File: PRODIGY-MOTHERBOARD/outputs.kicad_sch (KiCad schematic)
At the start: 19 parts, among them J10 GPIO, J11 SPI_OUT, J12 I2C, J13 CAN, J14 SERIAL, J15 12V OUT, J16 SERVO, J17 SERVO, J18 SERVO, J19 Ultrasonic, J20 MOTOR, J21 MOTOR, J3 A_IN, J4 USB_A, J5 A_OUT, J6 Neopixel, J7 GPIO, J8 GPIO, J9 GPIO

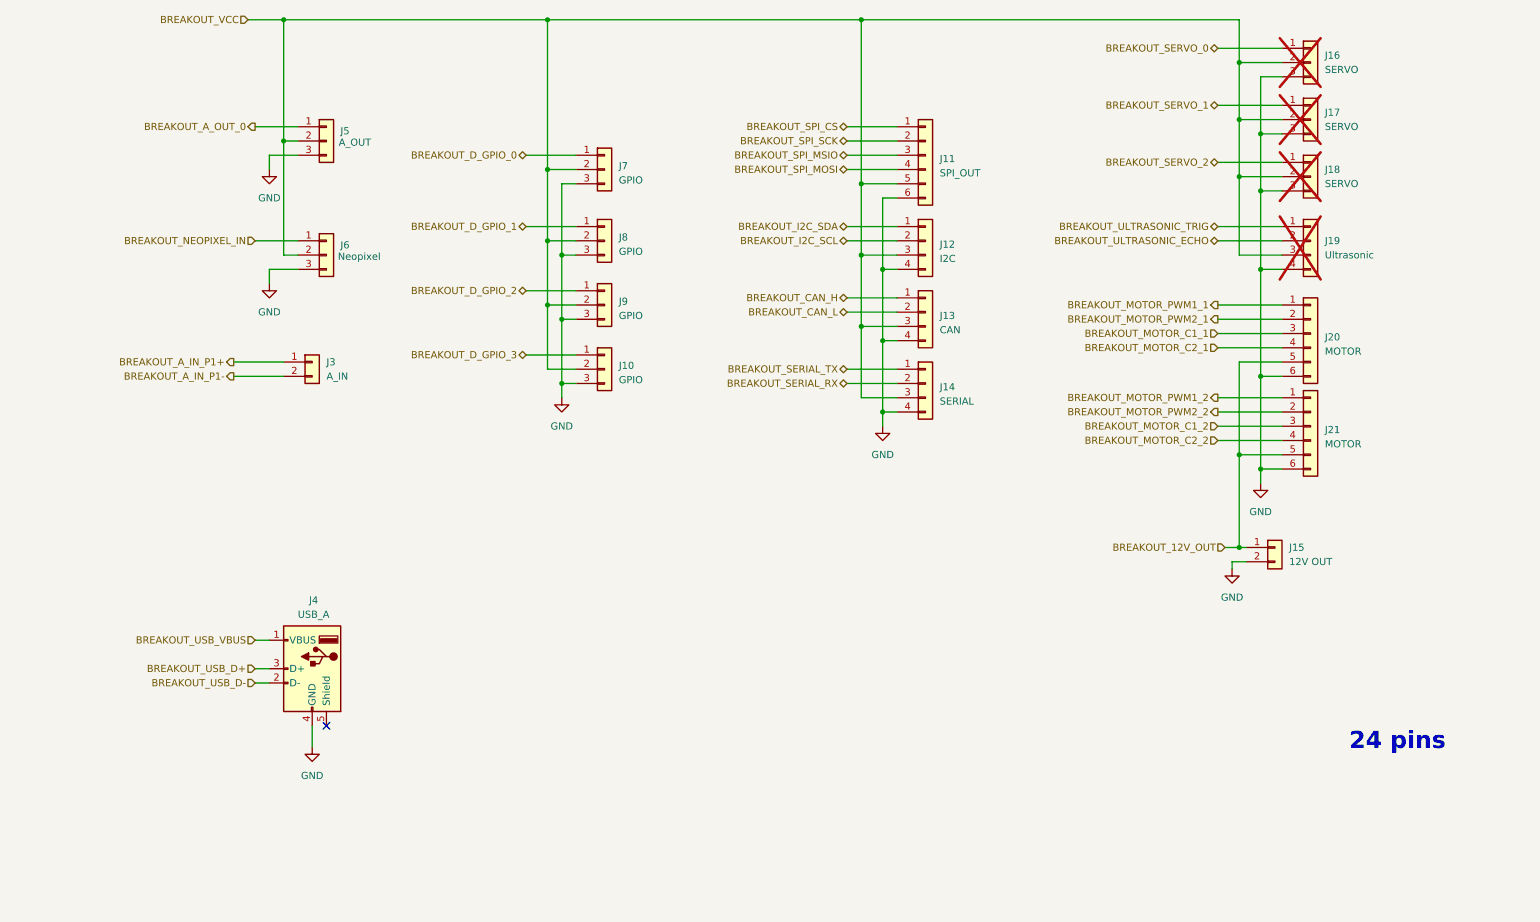
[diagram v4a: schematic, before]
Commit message: Analog schematic finished, except the joystick part.
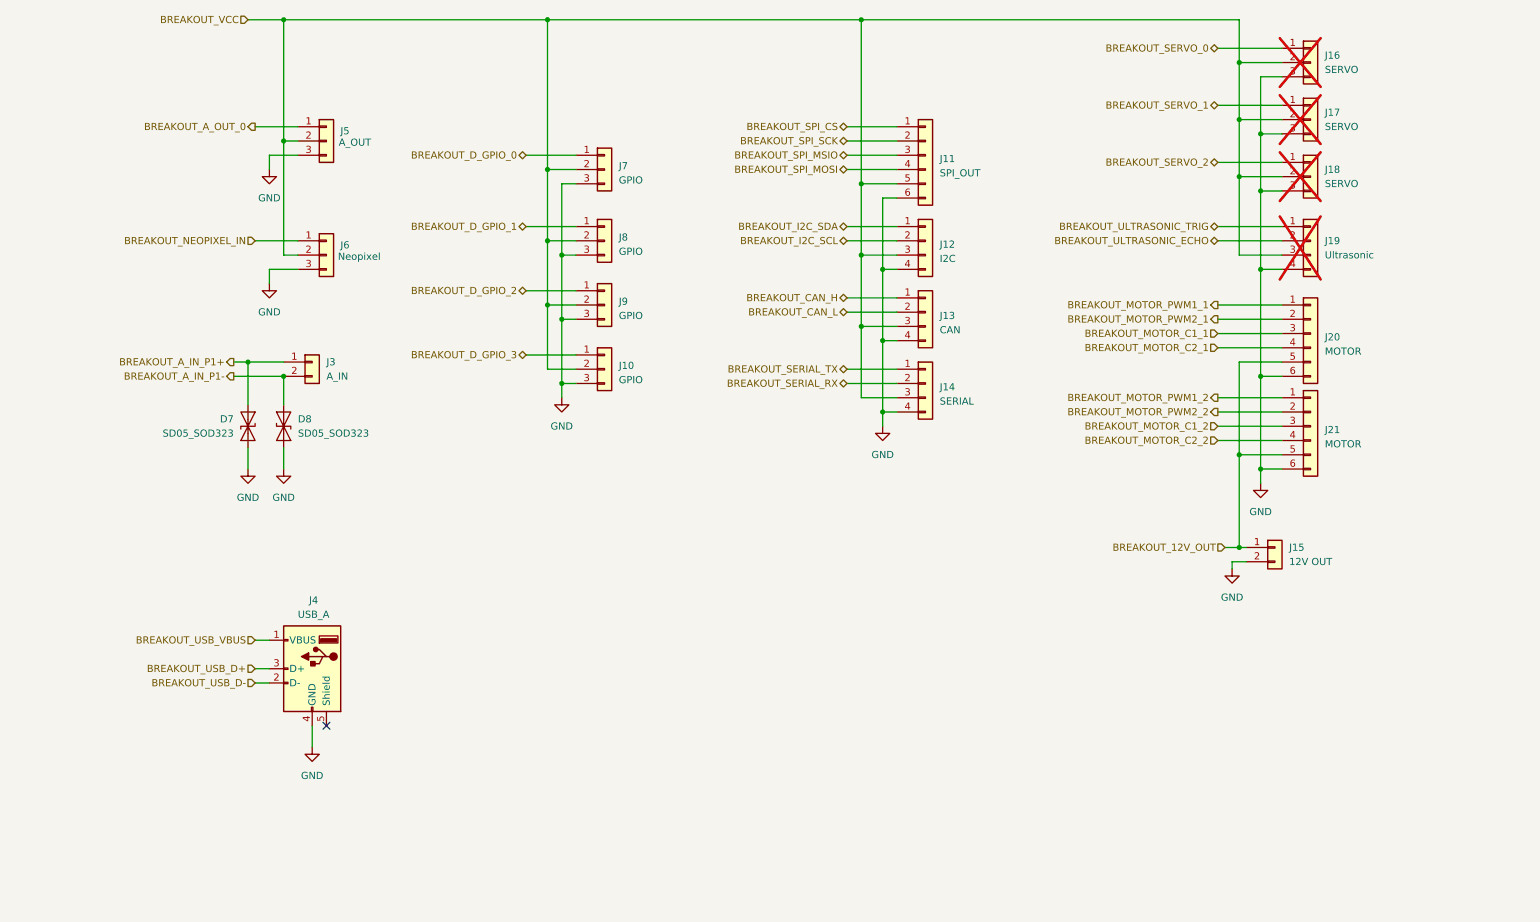
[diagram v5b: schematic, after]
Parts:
- added D7, D8: SD05_SOD323, Diode_SMD:D_SOD-323, symbol Diode:SD05_SOD323
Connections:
- net BREAKOUT_A_IN_P1+: now also D7.2 (A2)
- net BREAKOUT_A_IN_P1-: now also D8.2 (A2)
- net GND: now also D7.1 (A1), D8.1 (A1)
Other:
- note removed: "24 pins"

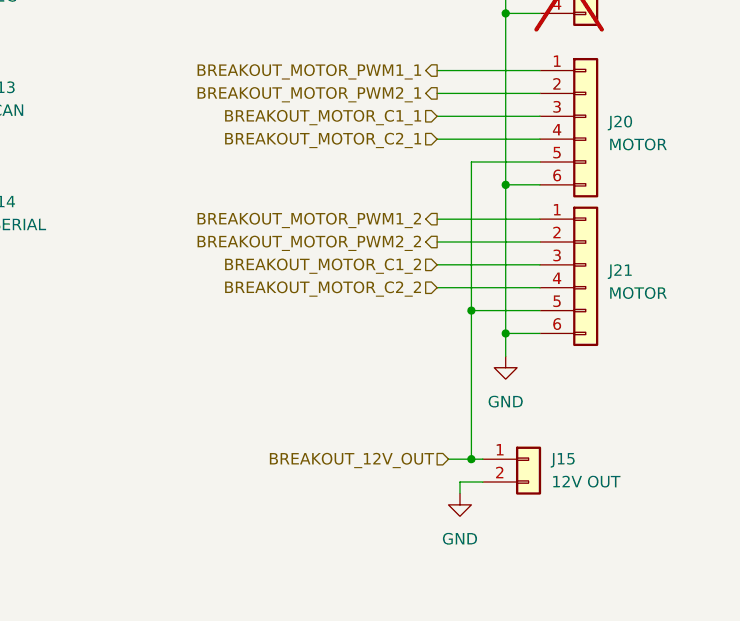
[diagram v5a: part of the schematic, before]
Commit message: Added pins to MCU. Added Decoder for SPI SS-Multiplexing.
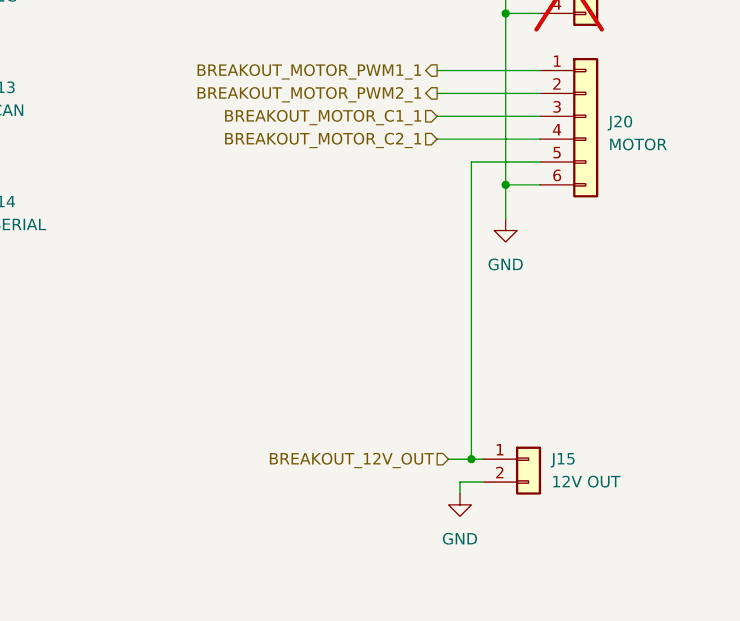
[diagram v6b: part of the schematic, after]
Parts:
- removed J21: MOTOR, Connector_JST:JST_XH_S6B-XH-A_1x06_P2.50mm_Horizontal, symbol Connector_Generic:Conn_01x06
- J16, J17, J18, J19: now left out of the parts list
